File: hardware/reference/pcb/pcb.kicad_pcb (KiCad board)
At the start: 2 copper layers, 125 x 72 mm, 64 parts, among them J1 POWER, J3 Conn_01x03, J4 Conn_02x03_Odd_Even, J5 485, J6 Conn_01x03, J7 SMA, SW1 SW_Push, U1 AMS1117-3.3, U2 AK09911C, U4 STM32F103C8Tx, U5 DS3231M, U6 NEO-M8M, Y1 8MHz, Y2 32.768kHz

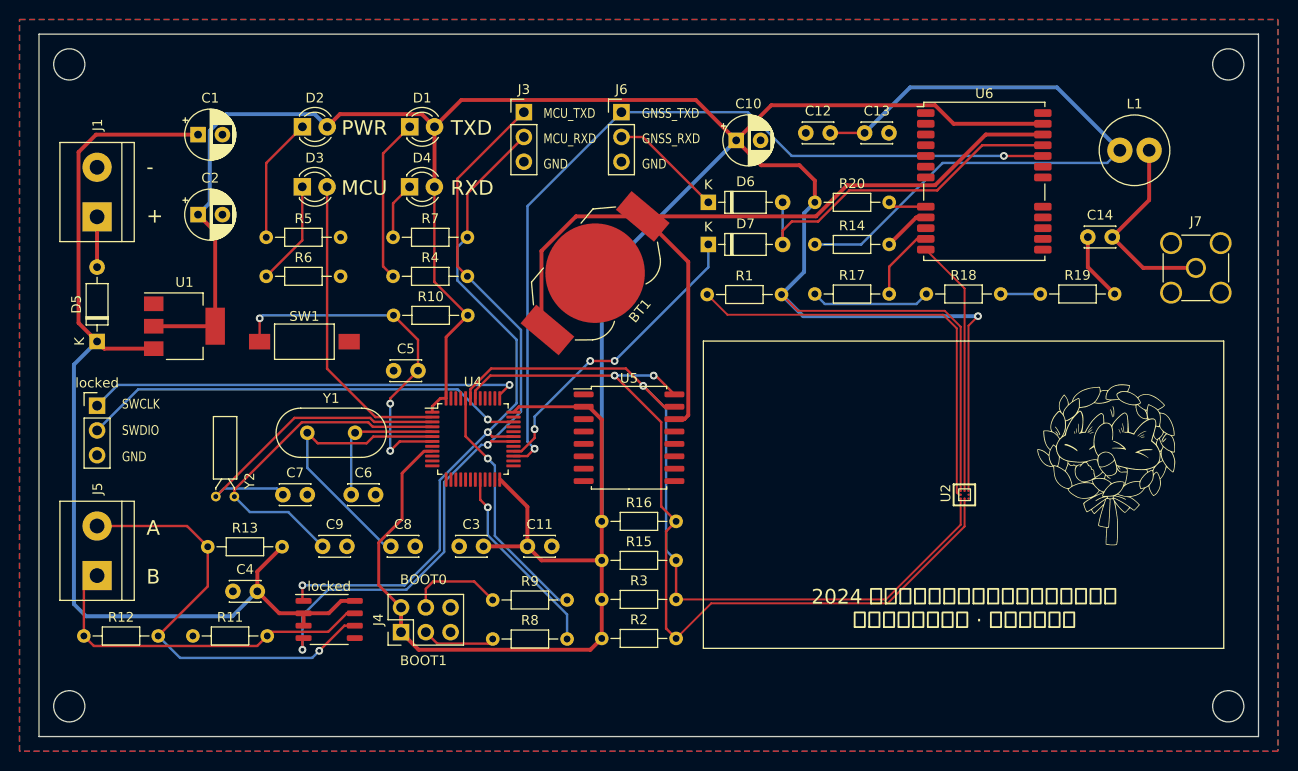
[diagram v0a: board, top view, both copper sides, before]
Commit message: Validate config fields
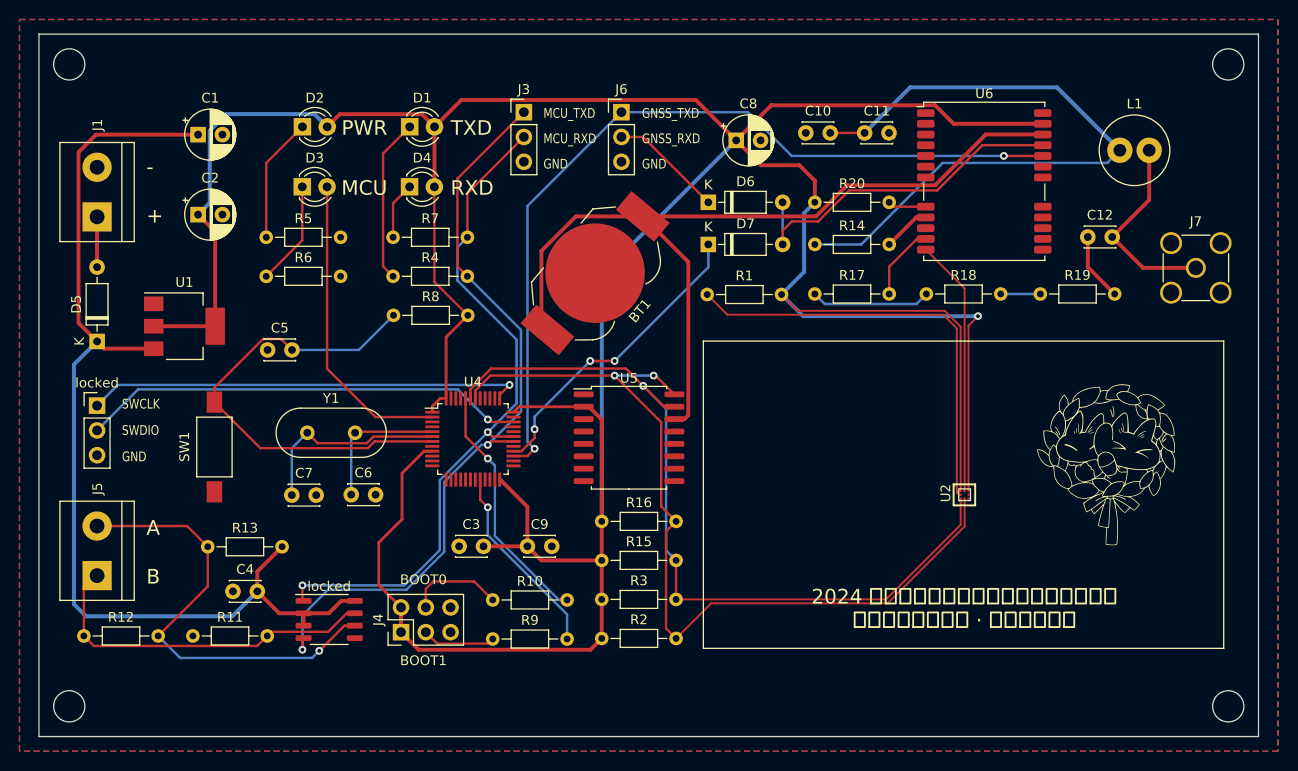
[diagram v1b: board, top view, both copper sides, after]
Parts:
- removed the C7 at (90.0, 92.7)
- removed the C9 at (94.1, 98.0)
- removed Y2: 32.768kHz, Crystal:Crystal_DS26_D2.0mm_L6.0mm_Horizontal
- moved SW1 14.2 mm to (83.0, 87.8), turned to -90 degrees
- moved C5 13.1 mm to (88.4, 77.9)
- moved C7 11.4 mm to (90.9, 92.8)
- renumbered C12 to C10, C13 to C11, C14 to C12, C8 to C7, C10 to C8, C11 to C9, R9 to R10, R10 to R8, R8 to R9
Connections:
- U4 pad 3: /MCU_OSC0 -> unconnected-(U4-PC14-Pad3)
- U4 pad 4: /MCU_OSC1 -> unconnected-(U4-PC15-Pad4)
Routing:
- net /MCU_OSC1: track 35.2 -> 0.00 mm
- net /MCU_OSC0: track 33.2 -> 0.00 mm
- net Net-(U4-NRST): track 37.1 -> 48.4 mm, vias 3 -> 0
- net /MCU_XTAL1: track 28.5 -> 20.6 mm
